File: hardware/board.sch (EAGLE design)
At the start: 44 parts, among them IC1 0915BM15A0001, J1 U.FL, U2 TPS63031, U3 BLE113-A, X1 CTS_32X25_SMD, X3 MINI-USB-UX60-MB-5ST

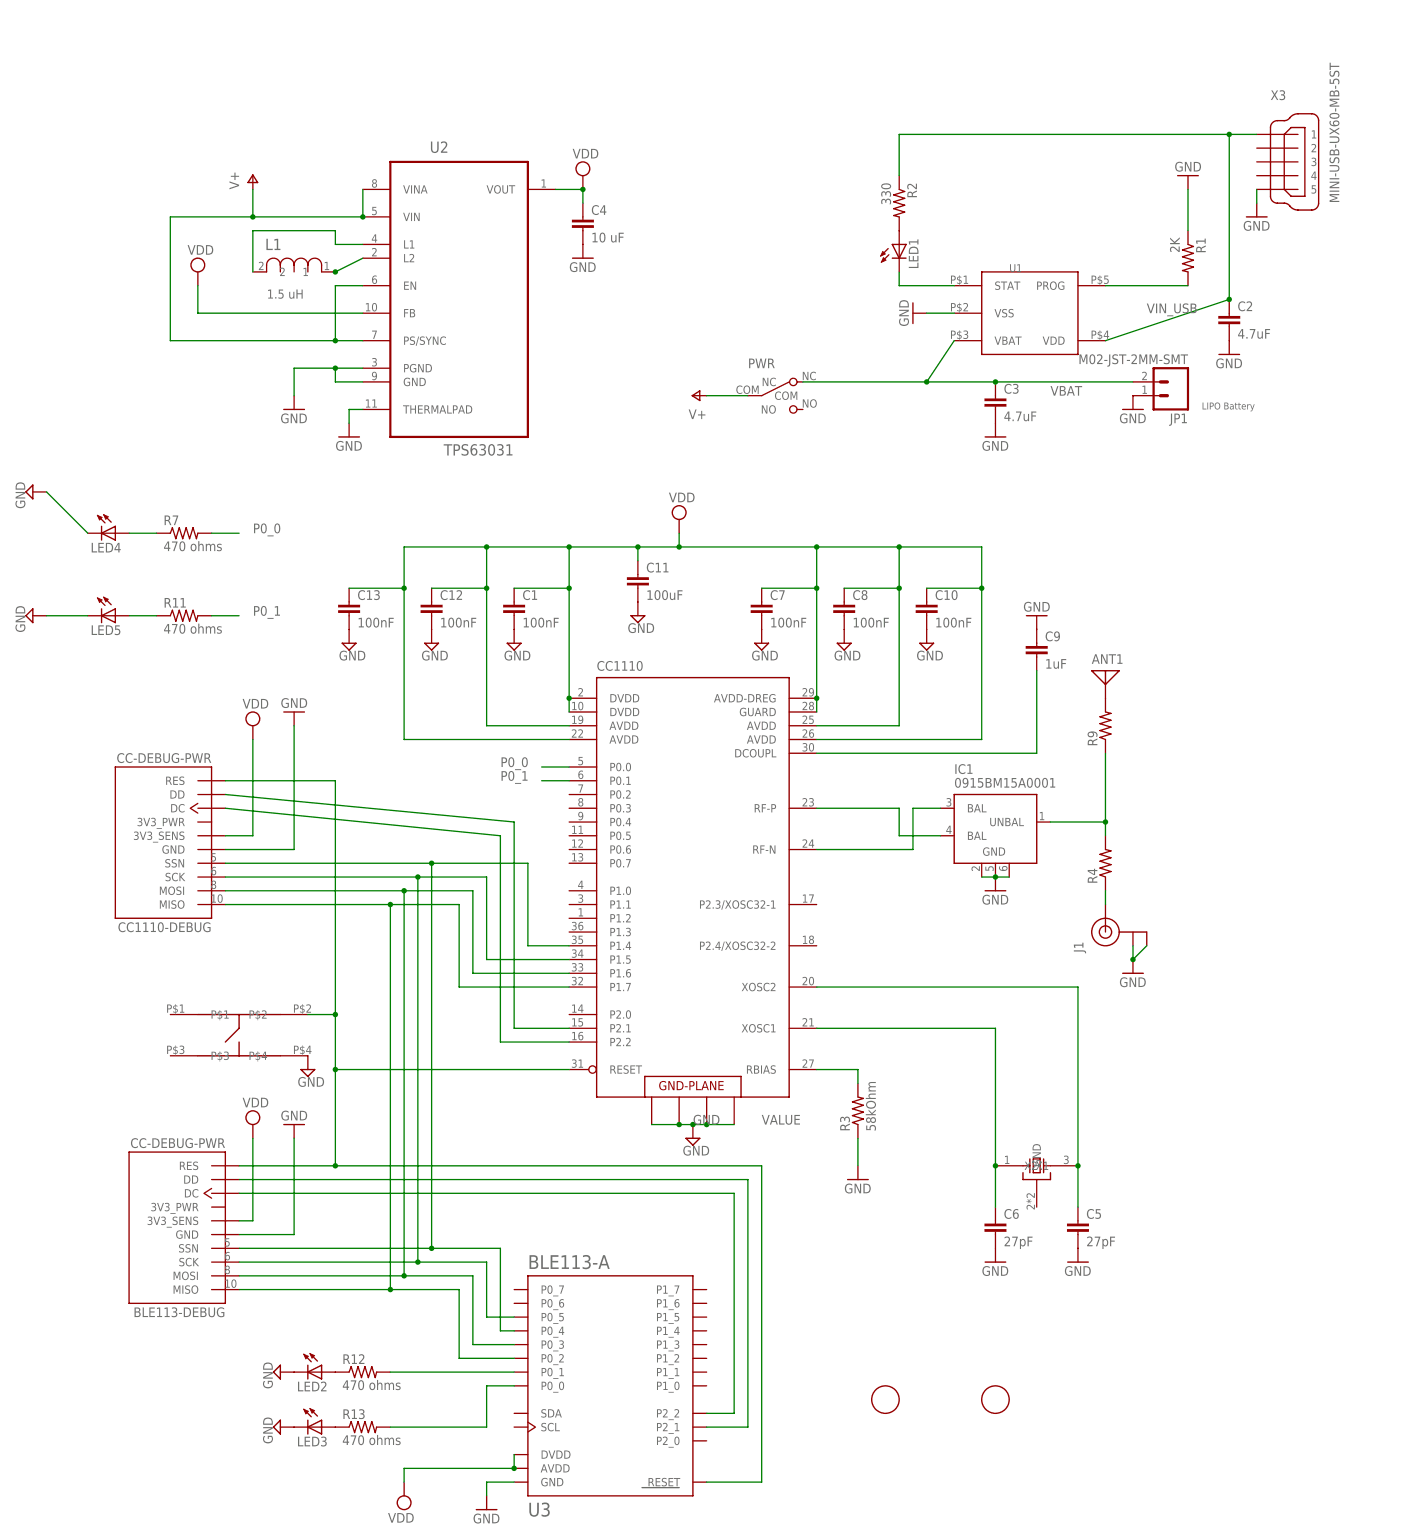
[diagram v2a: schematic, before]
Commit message: Rounded corners, align fiducials
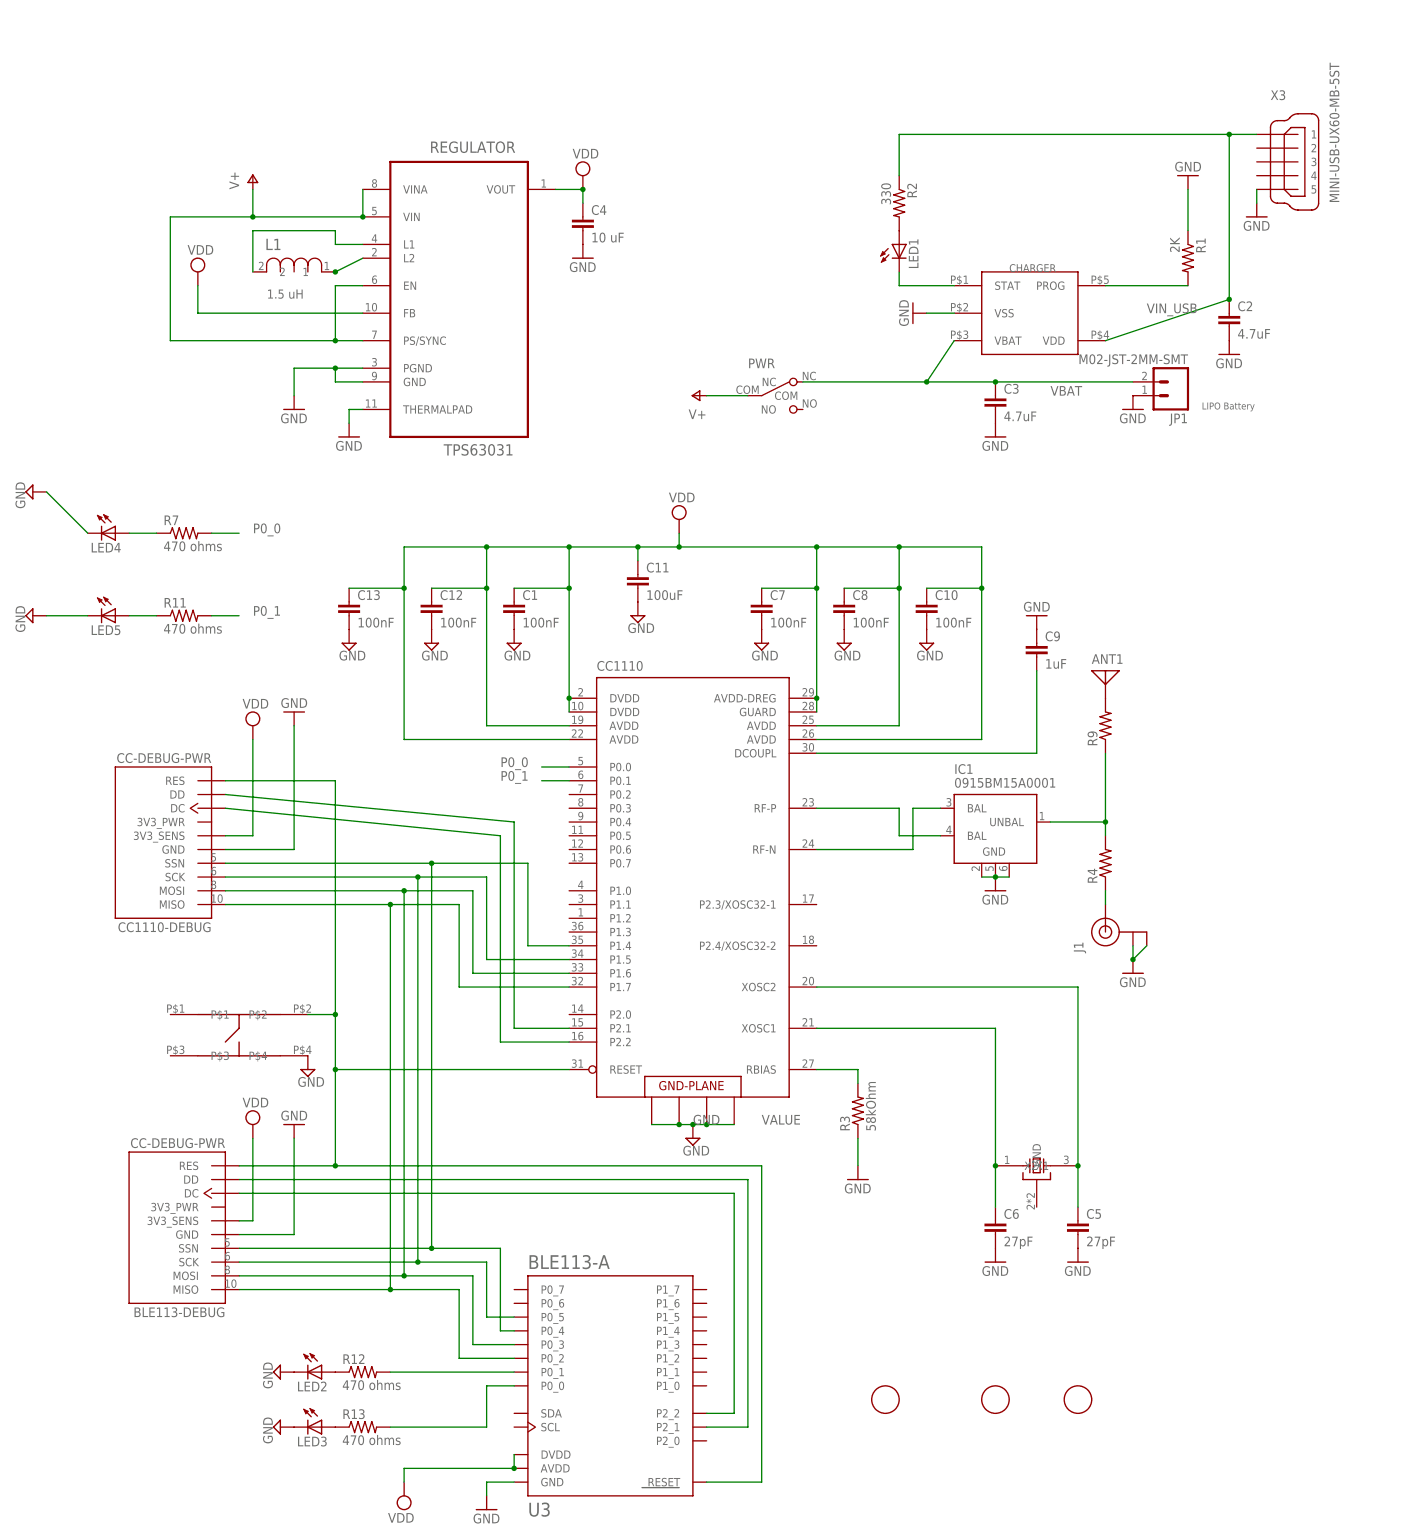
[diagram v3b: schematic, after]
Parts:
- added FID3: FIDUCIAL, adafruit:FIDUCIAL
- renumbered U$1 to FID1, U$3 to FID2, U1 to CHARGER, U2 to REGULATOR
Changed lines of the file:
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@@
 <part name="SUPPLY4" library="supply2" deviceset="GND" device=""/>
 <part name="SUPPLY1" library="supply2" deviceset="VDD" device=""/>
-<part name="U1" library="parts" deviceset="MCP73831" device=""/>
+<part name="CHARGER" library="parts" deviceset="MCP73831" device=""/>
 <part name="X3" library="con-hirose" deviceset="MINI-USB-" device="UX60-MB-5ST"/>
 <part name="JP1" library="SparkFun-Connectors" deviceset="M02" device="-JST-2MM-SMT"/>
@@
 <part name="GND5" library="supply1" deviceset="GND" device=""/>
 <part name="GND6" library="supply1" deviceset="GND" device=""/>
-<part name="U2" library="Texas Instruments_By_element14_Batch_1" deviceset="TPS63031" device="">
+<part name="REGULATOR" library="Texas Instruments_By_element14_Batch_1" deviceset="TPS63031" device="">
 <attribute name="MPN" value="TPS63031"/>
 </part>
@@
 <part name="SUPPLY18" library="supply2" deviceset="VDD" device=""/>
 <part name="GND20" library="supply1" deviceset="GND" device=""/>
-<part name="U$1" library="adafruit" deviceset="FIDUCIAL" device=""/>
-<part name="U$3" library="adafruit" deviceset="FIDUCIAL" device=""/>
+<part name="FID1" library="adafruit" deviceset="FIDUCIAL" device=""/>
+<part name="FID2" library="adafruit" deviceset="FIDUCIAL" device=""/>
+<part name="FID3" library="adafruit" deviceset="FIDUCIAL" device=""/>
 </parts>
 <sheets>
@@
 <instance part="SUPPLY4" gate="GND" x="43.18" y="88.9"/>
 <instance part="SUPPLY1" gate="G$1" x="73.66" y="111.76"/>
-<instance part="U1" gate="G$1" x="137.16" y="149.86"/>
+<instance part="CHARGER" gate="G$1" x="137.16" y="149.86"/>
 <instance part="X3" gate="G$1" x="185.42" y="177.8"/>
 <instance part="JP1" gate="G$1" x="165.1" y="137.16" rot="R180"/>
@@
 <instance part="GND5" gate="1" x="132.08" y="127"/>
 <instance part="GND6" gate="1" x="157.48" y="132.08"/>
-<instance part="U2" gate="A" x="33.02" y="154.94"/>
+<instance part="REGULATOR" gate="A" x="33.02" y="154.94"/>
 <instance part="GND7" gate="1" x="2.54" y="132.08"/>
 <instance part="GND8" gate="1" x="12.7" y="127"/>
@@
 <instance part="SUPPLY18" gate="G$1" x="22.86" y="-68.58" rot="R180"/>
 <instance part="GND20" gate="1" x="157.48" y="27.94"/>
-<instance part="U$1" gate="G$1" x="111.76" y="-50.8"/>
-<instance part="U$3" gate="G$1" x="132.08" y="-50.8"/>
+<instance part="FID1" gate="G$1" x="111.76" y="-50.8"/>
+<instance part="FID2" gate="G$1" x="132.08" y="-50.8"/>
+<instance part="FID3" gate="G$1" x="147.32" y="-50.8"/>
 </instances>
 <busses>
@@
 </segment>
 <segment>
-<pinref part="U1" gate="G$1" pin="VSS"/>
+<pinref part="CHARGER" gate="G$1" pin="VSS"/>
 <pinref part="GND4" gate="1" pin="GND"/>
 <wire x1="124.46" y1="149.86" x2="119.38" y2="149.86" width="0.1524" layer="91"/>
@@
 </segment>
 <segment>
-<pinref part="U2" gate="A" pin="PGND"/>
+<pinref part="REGULATOR" gate="A" pin="PGND"/>
 <wire x1="15.24" y1="139.7" x2="10.16" y2="139.7" width="0.1524" layer="91"/>
 <wire x1="10.16" y1="139.7" x2="10.16" y2="137.16" width="0.1524" layer="91"/>
-<pinref part="U2" gate="A" pin="GND"/>
+<pinref part="REGULATOR" gate="A" pin="GND"/>
 <wire x1="15.24" y1="137.16" x2="10.16" y2="137.16" width="0.1524" layer="91"/>
 <wire x1="10.16" y1="139.7" x2="2.54" y2="139.7" width="0.1524" layer="91"/>
@@
 </segment>
 <segment>
-<pinref part="U2" gate="A" pin="THERMALPAD"/>
+<pinref part="REGULATOR" gate="A" pin="THERMALPAD"/>
 <pinref part="GND8" gate="1" pin="GND"/>
 <wire x1="15.24" y1="132.08" x2="12.7" y2="132.08" width="0.1524" layer="91"/>
@@
 <net name="VDD" class="0">
 <segment>
-<pinref part="U2" gate="A" pin="VOUT"/>
+<pinref part="REGULATOR" gate="A" pin="VOUT"/>
 <pinref part="C4" gate="G$1" pin="1"/>
 <wire x1="50.8" y1="172.72" x2="55.88" y2="172.72" width="0.1524" layer="91"/>
@@
 </segment>
 <segment>
-<pinref part="U2" gate="A" pin="FB"/>
+<pinref part="REGULATOR" gate="A" pin="FB"/>
 <pinref part="SUPPLY3" gate="G$1" pin="VDD"/>
 <wire x1="15.24" y1="149.86" x2="-15.24" y2="149.86" width="0.1524" layer="91"/>
@@
 <net name="N$3" class="0">
 <segment>
-<pinref part="U1" gate="G$1" pin="PROG"/>
+<pinref part="CHARGER" gate="G$1" pin="PROG"/>
 <wire x1="152.4" y1="154.94" x2="167.64" y2="154.94" width="0.1524" layer="91"/>
 <pinref part="R1" gate="G$1" pin="2"/>
@@
 <net name="N$2" class="0">
 <segment>
-<pinref part="U1" gate="G$1" pin="STAT"/>
+<pinref part="CHARGER" gate="G$1" pin="STAT"/>
 <pinref part="LED1" gate="G$1" pin="C"/>
 <wire x1="124.46" y1="154.94" x2="114.3" y2="154.94" width="0.1524" layer="91"/>
@@
 <net name="VIN_USB" class="0">
 <segment>
-<pinref part="U1" gate="G$1" pin="VDD"/>
+<pinref part="CHARGER" gate="G$1" pin="VDD"/>
 <pinref part="C2" gate="G$1" pin="1"/>
 <wire x1="175.26" y1="152.4" x2="152.4" y2="144.78" width="0.1524" layer="91"/>
@@
 <net name="N$1" class="0">
 <segment>
-<pinref part="U2" gate="A" pin="L2"/>
+<pinref part="REGULATOR" gate="A" pin="L2"/>
 <pinref part="L1" gate="A" pin="1"/>
 <wire x1="10.16" y1="157.48" x2="15.24" y2="160.02" width="0.1524" layer="91"/>
@@
 <net name="N$6" class="0">
 <segment>
-<pinref part="U2" gate="A" pin="L1"/>
+<pinref part="REGULATOR" gate="A" pin="L1"/>
 <wire x1="15.24" y1="162.56" x2="10.16" y2="162.56" width="0.1524" layer="91"/>
 <wire x1="10.16" y1="162.56" x2="10.16" y2="165.1" width="0.1524" layer="91"/>
@@
 <net name="V+" class="0">
 <segment>
-<pinref part="U2" gate="A" pin="VIN"/>
-<pinref part="U2" gate="A" pin="VINA"/>
+<pinref part="REGULATOR" gate="A" pin="VIN"/>
+<pinref part="REGULATOR" gate="A" pin="VINA"/>
 <wire x1="15.24" y1="167.64" x2="15.24" y2="172.72" width="0.1524" layer="91"/>
 <wire x1="15.24" y1="167.64" x2="-5.08" y2="167.64" width="0.1524" layer="91"/>
@@
 <wire x1="-20.32" y1="167.64" x2="-20.32" y2="144.78" width="0.1524" layer="91"/>
 <junction x="15.24" y="167.64"/>
-<pinref part="U2" gate="A" pin="PS/SYNC"/>
+<pinref part="REGULATOR" gate="A" pin="PS/SYNC"/>
 <wire x1="-20.32" y1="144.78" x2="10.16" y2="144.78" width="0.1524" layer="91"/>
-<pinref part="U2" gate="A" pin="EN"/>
+<pinref part="REGULATOR" gate="A" pin="EN"/>
 <wire x1="10.16" y1="144.78" x2="15.24" y2="144.78" width="0.1524" layer="91"/>
 <wire x1="15.24" y1="154.94" x2="10.16" y2="154.94" width="0.1524" layer="91"/>
@@
 <net name="VBAT" class="0">
 <segment>
-<pinref part="U1" gate="G$1" pin="VBAT"/>
+<pinref part="CHARGER" gate="G$1" pin="VBAT"/>
 <wire x1="124.46" y1="144.78" x2="119.38" y2="137.16" width="0.1524" layer="91"/>
 <pinref part="C3" gate="G$1" pin="1"/>

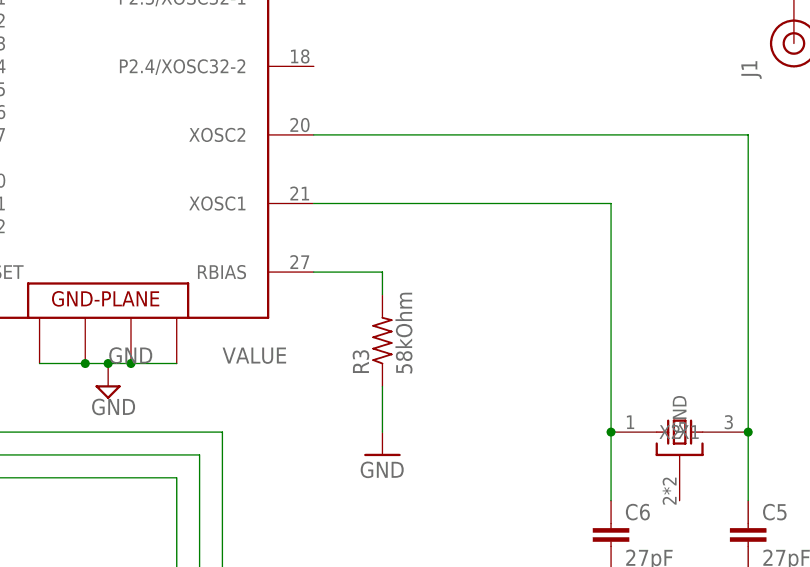
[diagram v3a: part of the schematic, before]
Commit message: Update value of bias resistor
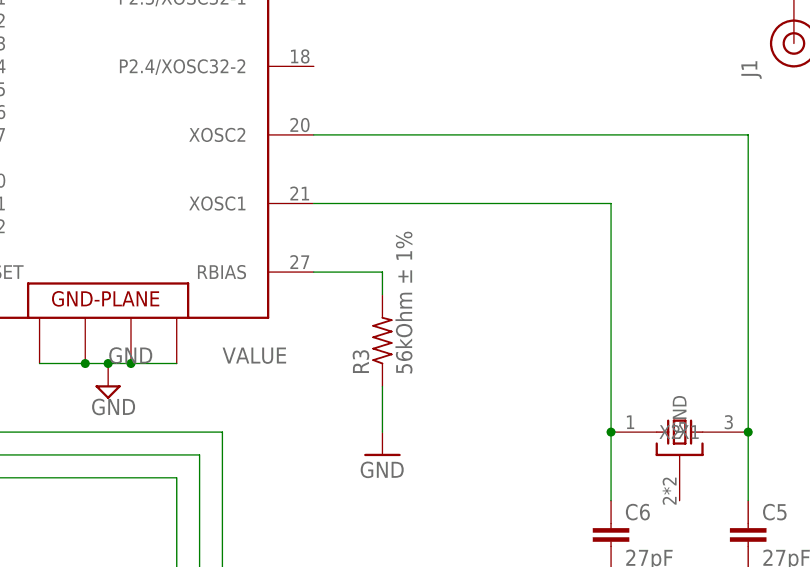
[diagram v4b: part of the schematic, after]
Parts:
- R3: value 58kOhm -> 56kOhm ± 1%
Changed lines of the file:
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@@
 <part name="GND15" library="supply1" deviceset="GND" device=""/>
 <part name="GND16" library="supply1" deviceset="GND" device=""/>
-<part name="R3" library="rcl" deviceset="R-US_" device="R0402" value="58kOhm"/>
+<part name="R3" library="rcl" deviceset="R-US_" device="R0402" value="56kOhm ± 1%"/>
 <part name="GND17" library="supply1" deviceset="GND" device=""/>
 <part name="C9" library="rcl" deviceset="C-EU" device="C0402K" value="1uF"/>

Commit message: Update crystal value and part number
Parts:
- X1: value CTS_32X25_SMD -> 26MHz 10pF 10ppm -20C +70C
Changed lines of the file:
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@@
 <parts>
 <part name="CC1110" library="parts" deviceset="CC1110" device=""/>
-<part name="X1" library="cts_crystal" deviceset="CTS_32X25_SMD" device=""/>
+<part name="X1" library="cts_crystal" deviceset="CTS_32X25_SMD" device="" value="26MHz 10pF 10ppm -20C +70C"/>
 <part name="C1" library="rcl" deviceset="C-EU" device="C0402" value="100nF"/>
 <part name="SUPPLY4" library="supply2" deviceset="GND" device=""/>
